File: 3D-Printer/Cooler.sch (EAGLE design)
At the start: 39 parts, among them IC1 L293D, IC2 REG1117

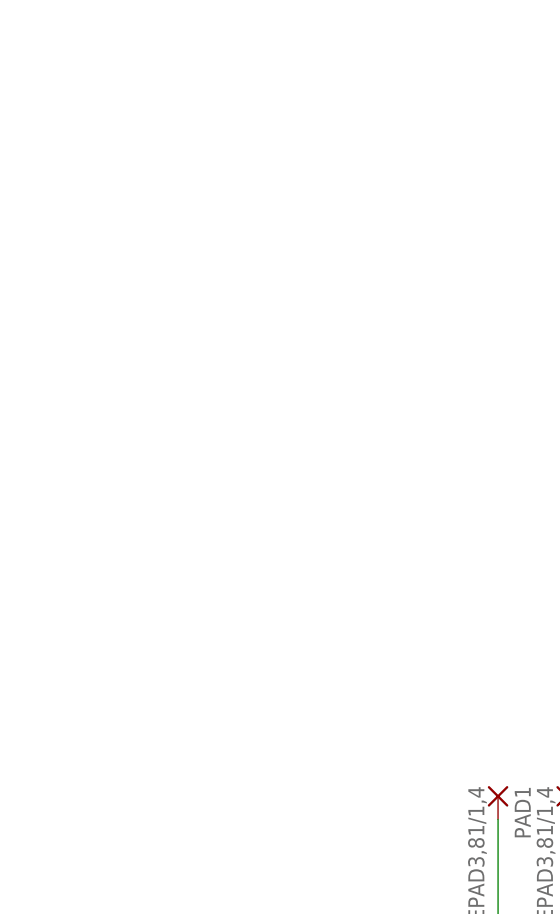
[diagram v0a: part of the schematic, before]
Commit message: correct meters
meters and serial needed reversed.
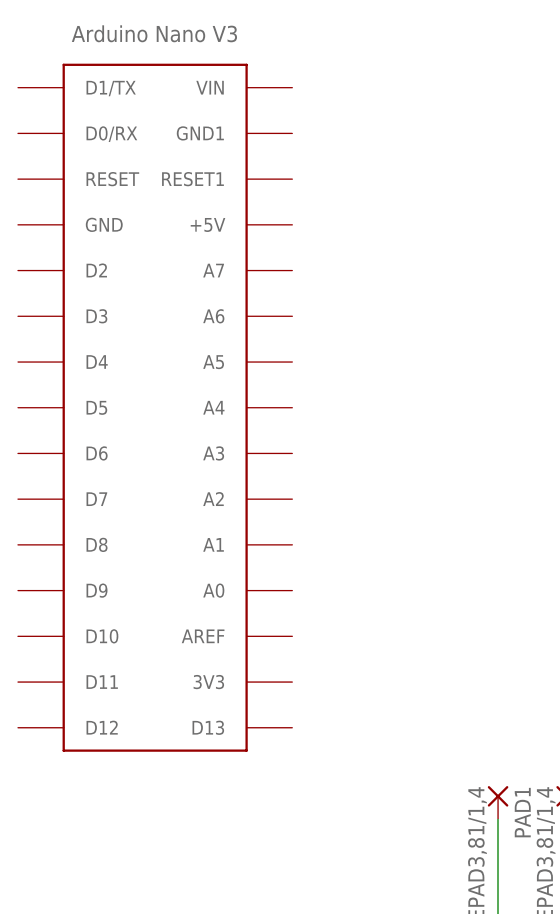
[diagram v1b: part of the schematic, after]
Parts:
- added U$2: ARDUINONANO, CRE-Lib1:ARDUINONANO
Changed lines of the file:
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@@
 <part name="PAD3" library="wirepad" deviceset="WIREPAD" device="3,81/1,4"/>
 <part name="CY5" library="resistor" deviceset="CY" device="YC7B5"/>
+<part name="U$2" library="CRE-Lib1" deviceset="ARDUINONANO" device=""/>
 </parts>
 <sheets>
@@
 <instance part="PAD3" gate="G$1" x="73.66" y="76.2" rot="R270"/>
 <instance part="CY5" gate="G$1" x="134.62" y="119.38" rot="R180"/>
+<instance part="U$2" gate="G$1" x="-40.64" y="177.8"/>
 </instances>
 <busses>

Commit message: Added bounce capacitor
Corrected bounce on switch
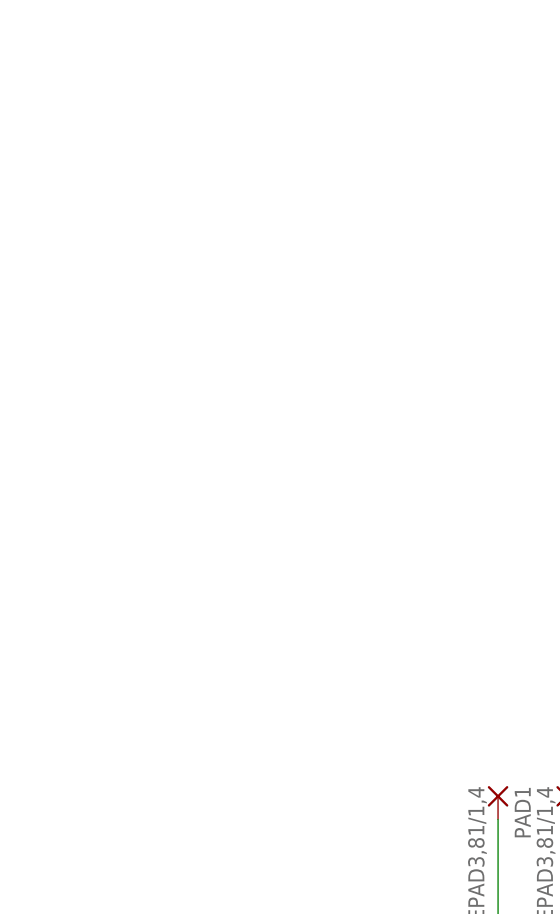
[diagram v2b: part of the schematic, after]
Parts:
- removed U$2: ARDUINONANO, CRE-Lib1:ARDUINONANO
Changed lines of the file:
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@@
 <grid distance="0.1" unitdist="inch" unit="inch" style="lines" multiple="1" display="no" altdistance="0.01" altunitdist="inch" altunit="inch"/>
 <layers>
-<layer number="1" name="Top" color="4" fill="1" visible="yes" active="no"/>
-<layer number="2" name="Route2" color="1" fill="3" visible="yes" active="no"/>
-<layer number="3" name="Route3" color="4" fill="3" visible="yes" active="no"/>
-<layer number="4" name="Route4" color="1" fill="4" visible="yes" active="no"/>
-<layer number="5" name="Route5" color="4" fill="4" visible="yes" active="no"/>
-<layer number="6" name="Route6" color="1" fill="8" visible="yes" active="no"/>
-<layer number="7" name="Route7" color="4" fill="8" visible="yes" active="no"/>
-<layer number="8" name="Route8" color="1" fill="2" visible="yes" active="no"/>
-<layer number="9" name="Route9" color="4" fill="2" visible="yes" active="no"/>
-<layer number="10" name="Route10" color="1" fill="7" visible="yes" active="no"/>
-<layer number="11" name="Route11" color="4" fill="7" visible="yes" active="no"/>
-<layer number="12" name="Route12" color="1" fill="5" visible="yes" active="no"/>
-<layer number="13" name="Route13" color="4" fill="5" visible="yes" active="no"/>
-<layer number="14" name="Route14" color="1" fill="6" visible="yes" active="no"/>
-<layer number="15" name="Route15" color="4" fill="6" visible="yes" active="no"/>
-<layer number="16" name="Bottom" color="1" fill="1" visible="yes" active="no"/>
-<layer number="17" name="Pads" color="2" fill="1" visible="yes" active="no"/>
-<layer number="18" name="Vias" color="2" fill="1" visible="yes" active="no"/>
-<layer number="19" name="Unrouted" color="6" fill="1" visible="yes" active="no"/>
-<layer number="20" name="Dimension" color="15" fill="1" visible="yes" active="no"/>
-<layer number="21" name="tPlace" color="7" fill="1" visible="yes" active="no"/>
-<layer number="22" name="bPlace" color="7" fill="1" visible="yes" active="no"/>
-<layer number="23" name="tOrigins" color="15" fill="1" visible="yes" active="no"/>
-<layer number="24" name="bOrigins" color="15" fill="1" visible="yes" active="no"/>
-<layer number="25" name="tNames" color="7" fill="1" visible="yes" active="no"/>
-<layer number="26" name="bNames" color="7" fill="1" visible="yes" active="no"/>
-<layer number="27" name="tValues" color="7" fill="1" visible="yes" active="no"/>
-<layer number="28" name="bValues" color="7" fill="1" visible="yes" active="no"/>
+<layer number="1" name="Top" color="4" fill="1" visible="no" active="no"/>
+<layer number="2" name="Route2" color="1" fill="3" visible="no" active="no"/>
+<layer number="3" name="Route3" color="4" fill="3" visible="no" active="no"/>
+<layer number="4" name="Route4" color="1" fill="4" visible="no" active="no"/>
+<layer number="5" name="Route5" color="4" fill="4" visible="no" active="no"/>
+<layer number="6" name="Route6" color="1" fill="8" visible="no" active="no"/>
+<layer number="7" name="Route7" color="4" fill="8" visible="no" active="no"/>
+<layer number="8" name="Route8" color="1" fill="2" visible="no" active="no"/>
+<layer number="9" name="Route9" color="4" fill="2" visible="no" active="no"/>
+<layer number="10" name="Route10" color="1" fill="7" visible="no" active="no"/>
+<layer number="11" name="Route11" color="4" fill="7" visible="no" active="no"/>
+<layer number="12" name="Route12" color="1" fill="5" visible="no" active="no"/>
+<layer number="13" name="Route13" color="4" fill="5" visible="no" active="no"/>
+<layer number="14" name="Route14" color="1" fill="6" visible="no" active="no"/>
+<layer number="15" name="Route15" color="4" fill="6" visible="no" active="no"/>
+<layer number="16" name="Bottom" color="1" fill="1" visible="no" active="no"/>
+<layer number="17" name="Pads" color="2" fill="1" visible="no" active="no"/>
+<layer number="18" name="Vias" color="2" fill="1" visible="no" active="no"/>
+<layer number="19" name="Unrouted" color="6" fill="1" visible="no" active="no"/>
+<layer number="20" name="Dimension" color="15" fill="1" visible="no" active="no"/>
+<layer number="21" name="tPlace" color="7" fill="1" visible="no" active="no"/>
+<layer number="22" name="bPlace" color="7" fill="1" visible="no" active="no"/>
+<layer number="23" name="tOrigins" color="15" fill="1" visible="no" active="no"/>
+<layer number="24" name="bOrigins" color="15" fill="1" visible="no" active="no"/>
+<layer number="25" name="tNames" color="7" fill="1" visible="no" active="no"/>
+<layer number="26" name="bNames" color="7" fill="1" visible="no" active="no"/>
+<layer number="27" name="tValues" color="7" fill="1" visible="no" active="no"/>
+<layer number="28" name="bValues" color="7" fill="1" visible="no" active="no"/>
 <layer number="29" name="tStop" color="7" fill="3" visible="no" active="no"/>
 <layer number="30" name="bStop" color="7" fill="6" visible="no" active="no"/>
@@
 <layer number="35" name="tGlue" color="7" fill="4" visible="no" active="no"/>
 <layer number="36" name="bGlue" color="7" fill="5" visible="no" active="no"/>
-<layer number="37" name="tTest" color="7" fill="1" visible="yes" active="no"/>
-<layer number="38" name="bTest" color="7" fill="1" visible="yes" active="no"/>
+<layer number="37" name="tTest" color="7" fill="1" visible="no" active="no"/>
+<layer number="38" name="bTest" color="7" fill="1" visible="no" active="no"/>
 <layer number="39" name="tKeepout" color="4" fill="11" visible="no" active="no"/>
 <layer number="40" name="bKeepout" color="1" fill="11" visible="no" active="no"/>
@@
 <layer number="44" name="Drills" color="7" fill="1" visible="no" active="no"/>
 <layer number="45" name="Holes" color="7" fill="1" visible="no" active="no"/>
-<layer number="46" name="Milling" color="3" fill="1" visible="yes" active="no"/>
-<layer number="47" name="Measures" color="7" fill="1" visible="yes" active="no"/>
-<layer number="48" name="Document" color="7" fill="1" visible="yes" active="no"/>
-<layer number="49" name="Reference" color="7" fill="1" visible="yes" active="no"/>
-<layer number="50" name="dxf" color="7" fill="1" visible="yes" active="no"/>
-<layer number="51" name="tDocu" color="7" fill="1" visible="yes" active="no"/>
-<layer number="52" name="bDocu" color="7" fill="1" visible="yes" active="no"/>
-<layer number="53" name="tGND_GNDA" color="7" fill="9" visible="yes" active="no"/>
-<layer number="54" name="bGND_GNDA" color="1" fill="9" visible="yes" active="no"/>
-<layer number="56" name="wert" color="7" fill="1" visible="yes" active="no"/>
-<layer number="57" name="tCAD" color="7" fill="1" visible="yes" active="no"/>
-<layer number="59" name="tCarbon" color="7" fill="1" visible="yes" active="no"/>
-<layer number="60" name="bCarbon" color="7" fill="1" visible="yes" active="no"/>
+<layer number="46" name="Milling" color="3" fill="1" visible="no" active="no"/>
+<layer number="47" name="Measures" color="7" fill="1" visible="no" active="no"/>
+<layer number="48" name="Document" color="7" fill="1" visible="no" active="no"/>
+<layer number="49" name="Reference" color="7" fill="1" visible="no" active="no"/>
+<layer number="50" name="dxf" color="7" fill="1" visible="no" active="no"/>
+<layer number="51" name="tDocu" color="7" fill="1" visible="no" active="no"/>
+<layer number="52" name="bDocu" color="7" fill="1" visible="no" active="no"/>
+<layer number="53" name="tGND_GNDA" color="7" fill="9" visible="no" active="no"/>
+<layer number="54" name="bGND_GNDA" color="1" fill="9" visible="no" active="no"/>
+<layer number="56" name="wert" color="7" fill="1" visible="no" active="no"/>
+<layer number="57" name="tCAD" color="7" fill="1" visible="no" active="no"/>
+<layer number="59" name="tCarbon" color="7" fill="1" visible="no" active="no"/>
+<layer number="60" name="bCarbon" color="7" fill="1" visible="no" active="no"/>
 <layer number="90" name="Modules" color="5" fill="1" visible="yes" active="yes"/>
 <layer number="91" name="Nets" color="2" fill="1" visible="yes" active="yes"/>
@@
 <part name="PAD3" library="wirepad" deviceset="WIREPAD" device="3,81/1,4"/>
 <part name="CY5" library="resistor" deviceset="CY" device="YC7B5"/>
-<part name="U$2" library="CRE-Lib1" deviceset="ARDUINONANO" device=""/>
 </parts>
 <sheets>
@@
 <instance part="PAD3" gate="G$1" x="73.66" y="76.2" rot="R270"/>
 <instance part="CY5" gate="G$1" x="134.62" y="119.38" rot="R180"/>
-<instance part="U$2" gate="G$1" x="-40.64" y="177.8"/>
 </instances>
 <busses>
